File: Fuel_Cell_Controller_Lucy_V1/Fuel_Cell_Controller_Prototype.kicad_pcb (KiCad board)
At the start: 2 copper layers, 114 parts, among them J1 STD_PWR_HEADER, J2 SWD_HEADER, J3 DE9_Receptacle, J4 DA15_Receptacle_MountingHoles, J5 USB_B_Micro, Q1 SI2302A-TPMSCT-ND, Q2 SI2302A-TPMSCT-ND, Q3 FMMT491ATA, Q4 FMMT491ATA, SW1 PTS815 SJM 250 SMTR LFS, SW2 PTS815 SJM 250 SMTR LFS, U1 LD39050PU33R, U10 FT234XD-R, U11 MCP2542FD-E/SN, U12 USBLC6-2SC6, U13 EL3H7(B)(TA)-VG, U14 MCP602-E/SN, U2 LD39050PU33R, U3 STM32L432KCUx, U4 MAX14572, U5 MAX14572, U6 EL3H7(B)(TA)-VG, U7 MCP1501-33E/SN, U8 AD8603, U9 AD8603, X1 OXETDLJANF-8MHZ

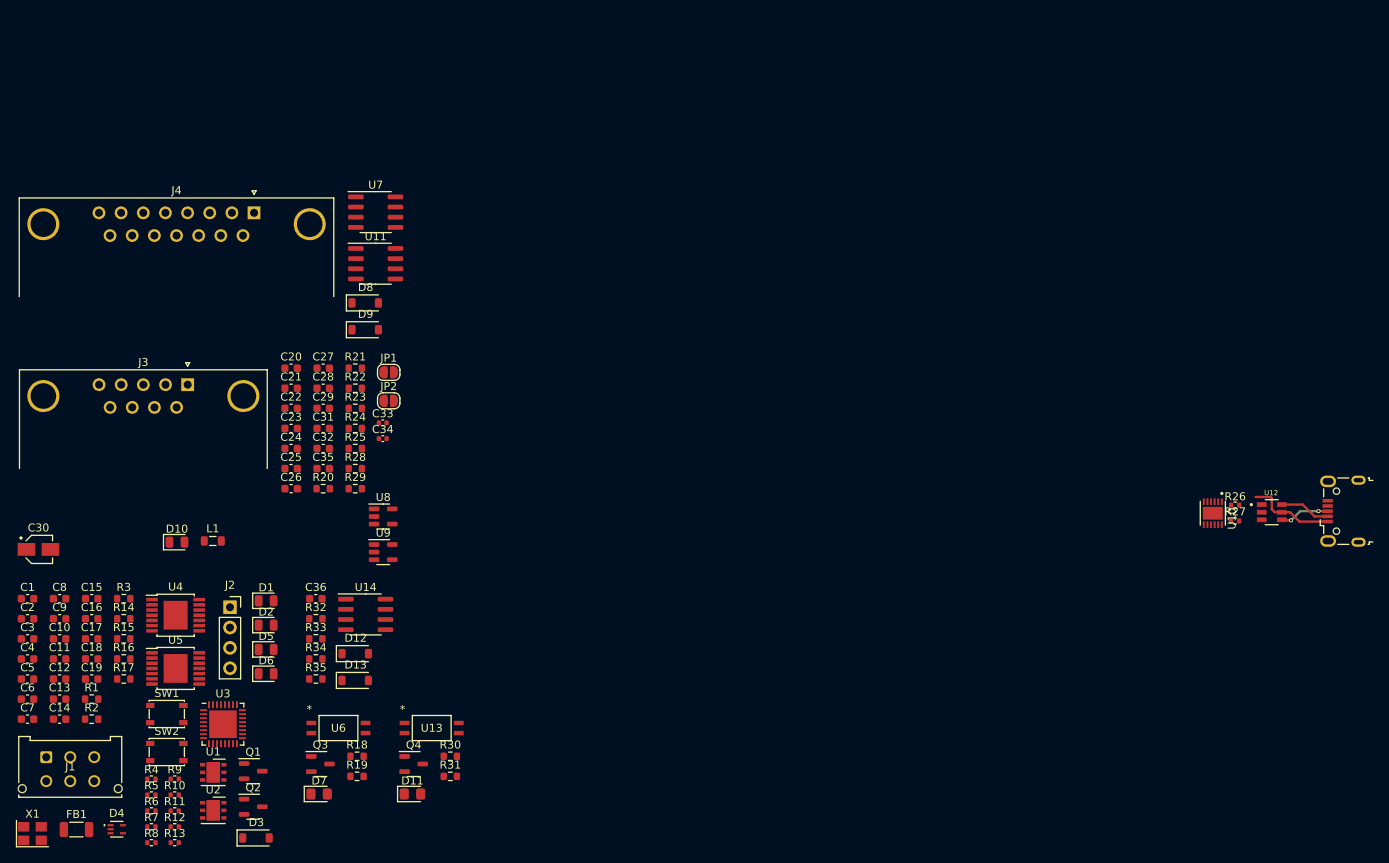
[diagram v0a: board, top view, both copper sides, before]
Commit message: Most of the schematic done, pcb layout needs DRC
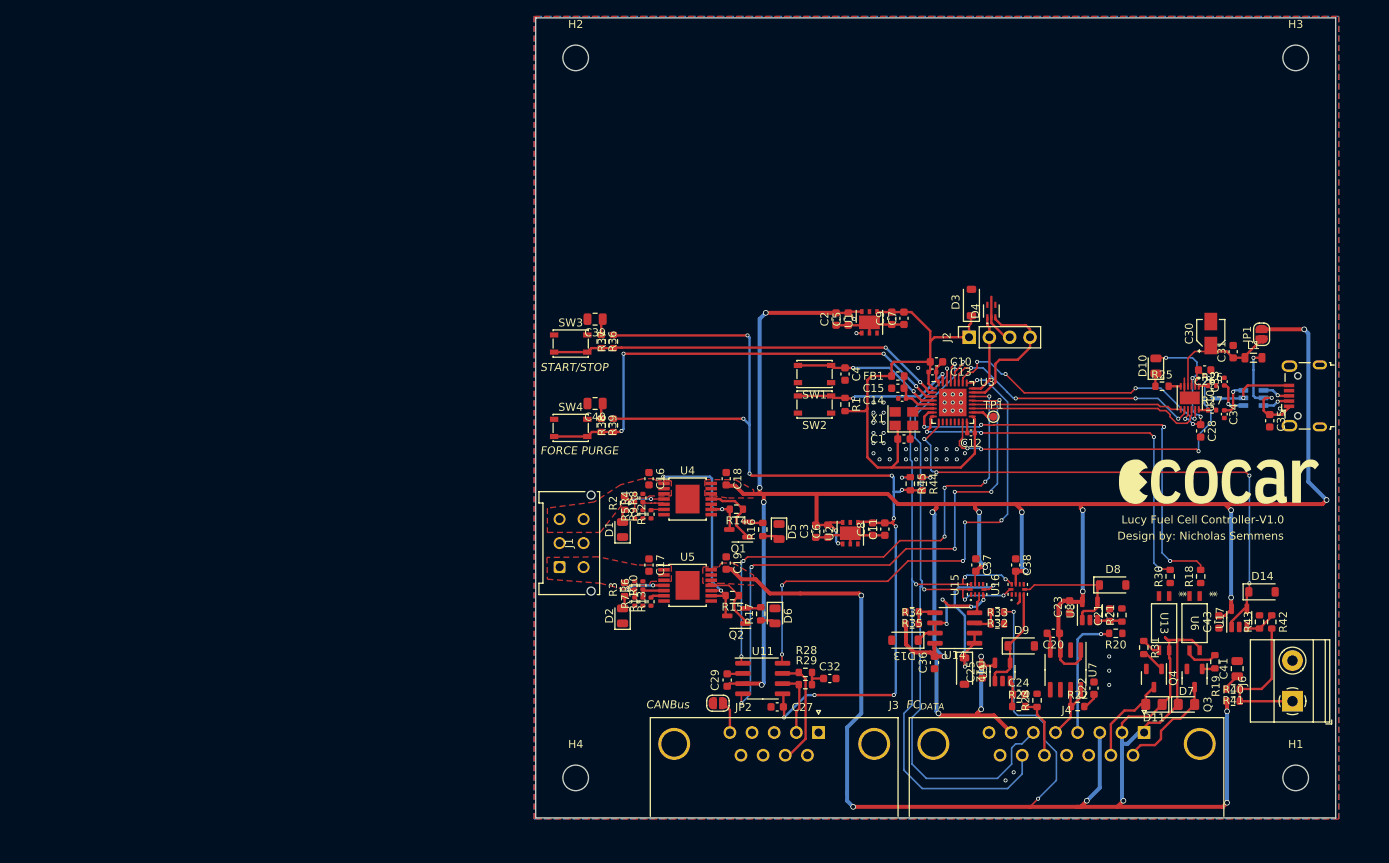
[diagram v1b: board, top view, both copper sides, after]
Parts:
- added C37: 100n, Capacitor_SMD:C_0603_1608Metric, F.Cu at (154.0, 104.4)
- added C38: 100n, Capacitor_SMD:C_0603_1608Metric, F.Cu at (159.0, 104.4)
- added C39: 3u, Capacitor_SMD:C_0805_2012Metric, F.Cu at (106.4, 73.7)
- added C40: 3u, Capacitor_SMD:C_0805_2012Metric, F.Cu at (106.4, 84.2)
- added C41: 3u, Capacitor_SMD:C_0805_2012Metric, F.Cu at (186.7, 117.3)
- added C43: 100n, Capacitor_SMD:C_0603_1608Metric, F.Cu at (184.4, 111.5)
- added D14: MMSZ5226B-7-F, FC.FTP:D_SOD_123_M, F.Cu at (189.7, 107.7)
- added G***: LOGO, RB_FTP:ecocar_logo, F.Cu at (184.4, 94.0)
- added H1: MountingHole, MountingHole:MountingHole_3.2mm_M3, F.Cu at (194.0, 131.0)
- added H2: MountingHole, MountingHole:MountingHole_3.2mm_M3, F.Cu at (104.0, 41.0)
- added H3: MountingHole, MountingHole:MountingHole_3.2mm_M3, F.Cu at (194.0, 41.0)
- added H4: MountingHole, MountingHole:MountingHole_3.2mm_M3, F.Cu at (104.0, 131.0)
- added J6: Screw_Terminal_01x02, TerminalBlock_Phoenix:TerminalBlock_Phoenix_MKDS-1,5-2-5.08_1x02_P5.08mm_Horizontal, F.Cu at (193.6, 121.4)
- added NT1: NetTie_2, NetTie:NetTie-2_SMD_Pad0.5mm, B.Cu at (184.2, 83.6)
- added R36: 10k, Resistor_SMD:R_0603_1608Metric, F.Cu at (107.2, 76.5)
- added R37: 10k, Resistor_SMD:R_0603_1608Metric, F.Cu at (108.7, 76.5)
- added R38: 10k, Resistor_SMD:R_0603_1608Metric, F.Cu at (108.7, 86.9)
- added R39: 10k, Resistor_SMD:R_0603_1608Metric, F.Cu at (107.2, 86.9)
- added R40: 10k, Resistor_SMD:R_0603_1608Metric, F.Cu at (186.2, 121.4)
- added R41: 10k, Resistor_SMD:R_0603_1608Metric, F.Cu at (186.2, 119.9)
- added R42: 1740, Resistor_SMD:R_0603_1608Metric, F.Cu at (191.0, 111.5)
- added R43: 660, Resistor_SMD:R_0603_1608Metric, F.Cu at (189.5, 111.5)
- added R44: 4.7k, Resistor_SMD:R_0603_1608Metric, F.Cu at (147.3, 94.2)
- added R45: 4.7k, Resistor_SMD:R_0603_1608Metric, F.Cu at (145.8, 94.2)
- added SW3: PTS815 SJM 250 SMTR LFS, Button_Switch_SMD:SW_SPST_PTS810, F.Cu at (103.4, 76.7)
- added SW4: PTS815 SJM 250 SMTR LFS, Button_Switch_SMD:SW_SPST_PTS810, F.Cu at (103.4, 87.3)
- added TP1: MCO, TestPoint:TestPoint_Pad_D1.0mm, F.Cu at (156.2, 85.9)
- added U15: ADS1115IRUGR, FC.FTP:IC_ADS1115IRUGR, F.Cu at (154.2, 107.4)
- added U16: ADS1115IRUGR, FC.FTP:IC_ADS1115IRUGR, F.Cu at (159.3, 107.4)
- added U17: AD8603, Package_TO_SOT_SMD:TSOT-23-5, F.Cu at (186.9, 111.0)
- C12, C13, C14: footprint Capacitor_SMD:C_0603_1608Metric -> Capacitor_SMD:C_0402_1005Metric
- C24: value 100n -> 1u
- FB1: footprint Inductor_SMD:L_1206_3216Metric -> Inductor_SMD:L_0603_1608Metric
- U12: moved to B.Cu
- moved C30 149.0 mm to (183.4, 75.5), turned to 90 degrees
- moved L1 132.1 mm to (188.7, 78.5)
- moved J4 128.8 mm to (175.1, 125.3)
- moved D4 127.1 mm to (156.0, 72.6), turned to 90 degrees
- moved D10 124.3 mm to (176.5, 79.5), turned to 90 degrees
- moved X1 120.6 mm to (145.0, 86.1)
- moved C7 120.5 mm to (145.0, 73.6), turned to 90 degrees
- moved C35 118.5 mm to (190.8, 86.4), turned to -90 degrees
- moved C12 118.0 mm to (153.4, 87.9), turned to 180 degrees
- moved FB1 117.3 mm to (144.3, 80.8)
- moved C13 116.5 mm to (148.6, 80.3)
- moved C26 115.2 mm to (182.6, 80.0), turned to 180 degrees
- moved C10 114.9 mm to (149.1, 79.0)
- moved C31 114.1 mm to (186.2, 77.7), turned to 90 degrees
- moved C14 112.7 mm to (144.8, 83.6), turned to 180 degrees
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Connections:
- net /On-Board Sensors/12V_Ref renamed /On-Board Sensors/12V_{REF}
- net /On-Board Sensors/5V_Ref renamed /On-Board Sensors/5V_{REF}
- C11 pad 1: GND -> GNDA
- C16 pad 1: GNDPWR -> GNDA
- C17 pad 1: GNDPWR -> GNDA
- C18 pad 1: GNDPWR -> GNDA
- C19 pad 1: GNDPWR -> GNDA
- C2 pad 1: GND -> GNDA
- C20 pad 2: GND -> GNDA
- C21 pad 2: GND -> GNDA
- C22 pad 2: GND -> GNDA
- C23 pad 1: GND -> GNDA
- C24 pad 2: GND -> GNDA
- C25 pad 1: GND -> GNDA
- C26 pad 1: GND -> GNDA
- C27 pad 2: GND -> GNDA
- C28 pad 2: GND -> GNDA
- C29 pad 1: GND -> GNDA
- C3 pad 1: GND -> GNDA
- C30 pad 2: GND -> GNDA
- C31 pad 2: GND -> GNDA
- C32 pad 1: GND -> GNDA
- C33 pad 2: GND -> GNDA
- C34 pad 2: GND -> GNDA
- C35 pad 2: GND -> GNDA
- C36 pad 1: GND -> GNDA
- C5 pad 1: GND -> GNDA
- C6 pad 1: GND -> GNDA
- C7 pad 1: GND -> GNDA
- C8 pad 1: GND -> GNDA
- C9 pad 1: GND -> GNDA
- D1 pad 1: GND -> GNDA
- D11 pad 1: UNPROTECTED_12V -> +12V
- D12 pad 2: GND -> GNDA
- D13 pad 2: GND -> GNDA
- D2 pad 1: GND -> GNDA
- D3 pad 1: +3V3 -> /MCU_3V3
- D4 pad 1: unconnected-(D4-Pad1) -> /IO /PA14
- D4 pad 3: unconnected-(D4-Pad3) -> /IO /PA13
- D4 pad 4: /IO /PA13 -> unconnected-(D4-Pad4)
- D4 pad 5: /IO /PA14 -> unconnected-(D4-Pad5)
- D5 pad 1: GND -> GNDA
- D6 pad 1: GND -> GNDA
- D7 pad 1: UNPROTECTED_12V -> +12V
- D8 pad 1: /IO /PA3 -> /IO /H2_{PRS}
- D8 pad 2: GND -> GNDA
- D9 pad 1: /IO /PA4 -> /IO /FC_{TEMP}
- D9 pad 2: GND -> GNDA
- J1 pad 2: GND -> GNDA
- J1 pad 5: GND -> GNDA
- J2 pad 1: +3V3 -> /MCU_3V3
- J3 pad 0: GND -> GNDA
- J3 pad 6: GND -> /IO /GND
- J4 pad 0: GND -> GNDA
- J4 pad 1: UNPROTECTED_12V -> +12V
- J4 pad 11: /IO /PRESSURE_PWR- -> GNDA
- J4 pad 14: unconnected-(J4-P14-Pad14) -> /IO /PB7
- J4 pad 15: GND -> GNDA
- J4 pad 2: UNPROTECTED_12V -> +12V
- J4 pad 3: /IO /PRESSURE_PWR+ -> +12V
- J4 pad 6: unconnected-(J4-Pad6) -> /IO /PB6
- J4 pad 7: unconnected-(J4-Pad7) -> +5V
- J4 pad 8: GND -> GNDA
- J5 pad 5: GND -> /IO /GND_{1}
- J5 pad 6: GND -> GNDA
- JP2 pad 1: GND -> GNDA
- R1 pad 1: +3V3 -> /BOOT0
- R1 pad 2: /BOOT0 -> /MCU_3V3
- R11 pad 1: GND -> GNDA
- R12 pad 1: GND -> GNDA
- R13 pad 1: GND -> GNDA
- R21 pad 2: GND -> GNDA
- R23 pad 2: GND -> GNDA
- R33 pad 2: GND -> GNDA
- R35 pad 2: GND -> GNDA
- R5 pad 1: GND -> GNDA
- R7 pad 1: GND -> GNDA
- R9 pad 1: GND -> GNDA
- U1 pad 2: GND -> GNDA
- U1 pad 7: GND -> GNDA
- U10 pad 13: GND -> GNDA
- U10 pad 5: GND -> GNDA
- U11 pad 2: GND -> GNDA
- U12 pad 2: GND -> /IO /GND_{1}
- U13 pad 4: UNPROTECTED_12V -> +12V
- U14 pad 4: GND -> GNDA
- U2 pad 2: GND -> GNDA
- U2 pad 7: GND -> GNDA
- U3 pad 2: unconnected-(U3-PC14-Pad2) -> /PC14
- U3 pad 3: unconnected-(U3-PC15-Pad3) -> /PC15
- U4 pad 15: GND -> GNDA
- U4 pad 7: GND -> GNDA
- U4 pad 8: GND -> GNDA
- U5 pad 10: UNPROTECTED_12V -> UNPROTECTED_5V
- U5 pad 15: GND -> GNDA
- U5 pad 7: GND -> GNDA
- U5 pad 8: GND -> GNDA
- U5 pad 9: UNPROTECTED_12V -> UNPROTECTED_5V
- U6 pad 4: UNPROTECTED_12V -> +12V
- U7 pad 2: GND -> GNDA
- U7 pad 4: GND -> GNDA
- U7 pad 5: GND -> GNDA
- U7 pad 6: GND -> GNDA
- U8 pad 1: /IO /PA3 -> /IO /H2_{PRS}
- U8 pad 2: GND -> GNDA
- U8 pad 4: /IO /PA3 -> /IO /H2_{PRS}
- U9 pad 1: /IO /PA4 -> /IO /FC_{TEMP}
- U9 pad 2: GND -> GNDA
- U9 pad 4: /IO /PA4 -> /IO /FC_{TEMP}
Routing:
- net +5V: track 0.00 -> 304.1 mm, vias 0 -> 23
- net +12V: track 0.00 -> 196.4 mm, vias 0 -> 8
- net +3V3: track 0.00 -> 123.3 mm, vias 0 -> 10
- net /IO /PB6: track 0.00 -> 91.8 mm, vias 0 -> 5
- net /IO /PB7: track 0.00 -> 90.7 mm, vias 0 -> 5
- net /IO /PA11: track 0.00 -> 72.2 mm, vias 0 -> 6
- net /MCU_3V3: track 0.00 -> 70.5 mm
- net /IO /PA3: track 0.00 -> 67.3 mm, vias 0 -> 4
- net /IO /PA15: track 0.00 -> 64.7 mm, vias 0 -> 6
- net /IO /PA12: track 0.00 -> 63.9 mm, vias 0 -> 6
- net /PC15: track 0.00 -> 59.4 mm, vias 0 -> 4
- net /IO /PA1: track 0.00 -> 54.7 mm, vias 0 -> 4
- net /PC14: track 0.00 -> 50.1 mm, vias 0 -> 2
- net /IO /PA2: track 0.00 -> 49.1 mm, vias 0 -> 4
- net /IO /PB1: track 0.00 -> 47.5 mm, vias 0 -> 4
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- added copper zone on F.Cu, net +12V
- added copper zone on F.Cu, net +5V
- added copper zone on B.Cu, net GNDA
- added copper zone on F.Cu, net GNDA
- added copper zone on F.Cu, net UNPROTECTED_12V
- added copper zone on F.Cu, net UNPROTECTED_5V
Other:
- board outline added: 100 x 100 mm
- board text added: "${COMMENT1}"
- board text added: "${TITLE}-${REVISION}"
- board text added: "CANBus"
- board text added: "FC_{DATA}"
- board text added: "FORCE PURGE"
- board text added: "START/STOP"

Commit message: So much again
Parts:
- added C42: 100n, Capacitor_SMD:C_0603_1608Metric, F.Cu at (133.8, 90.6)
- added C45: 10u, Capacitor_SMD:CP_Elec_3x5.3, F.Cu at (130.6, 88.1)
- added Display 128x64 0.96" I2C: Display_128x64, FC.FTP:Display_128x64_096_I2C, F.Cu at (166.4, 92.5)
- added J7: OLED, Connector_PinSocket_2.54mm:PinSocket_1x04_P2.54mm_Vertical, F.Cu at (162.6, 92.4)
- added U18: LIS3DHTR, FC.FTP:XDCR_LIS3DHTR, F.Cu at (137.1, 89.6)
- moved G*** 67.1 mm to (123.0, 67.0)
- moved H2 28.0 mm to (104.0, 69.0)
- moved H3 28.0 mm to (194.0, 69.0)
- moved C1 3.02 mm to (142.1, 87.9), turned to -90 degrees
- moved D3 2.13 mm to (151.8, 73.0), turned to 180 degrees
- moved C39 1.74 mm to (108.2, 73.9), turned to 0 degrees
- moved C40 1.73 mm to (108.2, 84.4), turned to 0 degrees
- moved C28 0.25 mm to (182.4, 87.6)
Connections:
- net /PC14 renamed /BTN_{1}
- net /PC15 renamed /BTN_{2}
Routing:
- net /IO /PB6: track 91.8 -> 128.7 mm, vias 5 -> 6
- net /IO /PB7: track 90.7 -> 127.4 mm, vias 5 -> 6
- net +5V: track 304.1 -> 325.5 mm, vias 23 -> 28
- net /IO /PA4: track 0.00 -> 19.4 mm, vias 0 -> 2
- net /IO /PA5: track 0.00 -> 16.8 mm, vias 0 -> 2
- net +3V3: track 123.3 -> 138.1 mm
- net /BOOT0: track 20.6 -> 30.9 mm, vias 2 -> 4
- net /MCU_3V3: track 70.5 -> 60.4 mm, vias 0 -> 4
- net /IO /PB5: track 3.06 -> 0.00 mm, vias 1 -> 0
- net /IO /PB4: track 33.1 -> 35.4 mm
- net GNDA: track 44.0 -> 46.0 mm, vias 44 -> 218
- net Net-(R30-Pad1): track 0.00 -> 1.68 mm
- net Net-(R18-Pad1): track 0.00 -> 1.68 mm
- net Net-(U8-+): track 3.03 -> 4.52 mm
- net /On-Board Sensors/5V_{REF}: track 15.0 -> 16.4 mm
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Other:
- board size 100 x 100 mm -> 100 x 73 mm
- board text added: "BOOT0"
- board text added: "~{RST}"

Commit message: $
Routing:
- net /MCU_3V3: track 60.4 -> 61.1 mm, vias 4 -> 5
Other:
- board text added: "~{FAULT}"
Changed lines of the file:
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@@
     (effects (font (size 1 1) (thickness 0.15) italic) (justify left bottom))
+  )
+  (gr_text "~{FAULT}" (at 131.953 113.157 90) (layer "F.SilkS")
+    (effects (font (size 1 1) (thickness 0.2) bold italic) (justify left bottom))
   )
   (gr_text "${COMMENT1}" (at 110.3 74.366) (layer "F.SilkS")
@@
   (gr_text "CANBus" (at 112.776 122.428) (layer "F.SilkS")
     (effects (font (size 1 1) (thickness 0.15) italic) (justify left bottom))
+  )
+  (gr_text "~{FAULT}" (at 132.461 102.489 90) (layer "F.SilkS")
+    (effects (font (size 1 1) (thickness 0.2) bold italic) (justify left bottom))
   )
   (gr_text "FORCE PURGE" (at 99.568 90.678) (layer "F.SilkS")
@@
   (segment (start 141.723 72.776) (end 141.666 72.719) (width 0.3) (layer "F.Cu") (net 1))
   (segment (start 143.4845 79.2735) (end 143.4845 80.772) (width 0.3) (layer "F.Cu") (net 1))
+  (segment (start 149.391 75.145) (end 148.323 75.145) (width 0.3) (layer "F.Cu") (net 1))
   (segment (start 153.172 73.1185) (end 153.3671 72.9234) (width 0.3) (layer "F.Cu") (net 1))
   (segment (start 148.3234 75.921) (end 148.323 75.9206) (width 0.3) (layer "F.Cu") (net 1))
   (segment (start 153.172 75.921) (end 153.172 73.1185) (width 0.3) (layer "F.Cu") (net 1))
+  (segment (start 149.86 74.676) (end 149.391 75.145) (width 0.3) (layer "F.Cu") (net 1))
   (segment (start 137.6802 85.1408) (end 137.668 85.153) (width 0.3) (layer "F.Cu") (net 1))
   (segment (start 148.11 81.7415) (end 148.6925 82.324) (width 0.3) (layer "F.Cu") (net 1))
@@
   (segment (start 148.323 75.145) (end 145.954 72.776) (width 0.3) (layer "F.Cu") (net 1))
   (segment (start 148.323 76.454) (end 148.323 75.145) (width 0.3) (layer "F.Cu") (net 1))
-  (segment (start 153.172 75.921) (end 148.3234 75.921) (width 0.3) (layer "F.Cu") (net 1))
   (segment (start 143.781 87.109) (end 143.934 86.956) (width 0.3) (layer "F.Cu") (net 1))
   (via (at 140.462 80.772) (size 0.5) (drill 0.3) (layers "F.Cu" "B.Cu") (net 1))
+  (via (at 149.86 74.676) (size 0.8) (drill 0.4) (layers "F.Cu" "B.Cu") (net 1))
   (via (at 153.8732 86.487) (size 0.5) (drill 0.3) (layers "F.Cu" "B.Cu") (net 1))
   (via (at 140.462 85.1408) (size 0.5) (drill 0.3) (layers "F.Cu" "B.Cu") (net 1))
@@
   (segment (start 140.462 80.772) (end 140.462 85.1408) (width 0.3) (layer "B.Cu") (net 1))
   (segment (start 153.172 75.921) (end 153.172 85.7858) (width 0.2) (layer "B.Cu") (net 1))
+  (segment (start 149.86 74.676) (end 150.114 74.676) (width 0.3) (layer "B.Cu") (net 1))
+  (segment (start 150.114 74.676) (end 151.359 75.921) (width 0.3) (layer "B.Cu") (net 1))
   (segment (start 140.462 86.995) (end 140.589 87.122) (width 0.3) (layer "B.Cu") (net 1))
   (segment (start 153.172 85.7858) (end 153.8732 86.487) (width 0.2) (layer "B.Cu") (net 1))
+  (segment (start 151.359 75.921) (end 153.172 75.921) (width 0.3) (layer "B.Cu") (net 1))
   (segment (start 138.176 87.249) (end 138.303 87.63) (width 0.3) (layer "F.Cu") (net 2))
   (segment (start 159.258 109.22) (end 159.508 108.97) (width 0.3) (layer "F.Cu") (net 2))

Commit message: I really shouldn't be pushing so much but oh well
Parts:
- added C44: 3u, Capacitor_SMD:C_0805_2012Metric, F.Cu at (184.7, 101.2)
- added J8: Screw_Terminal_01x02, TerminalBlock_Phoenix:TerminalBlock_Phoenix_MKDS-1,5-2-5.08_1x02_P5.08mm_Horizontal, F.Cu at (193.8, 103.0)
- added R47: 10k, Resistor_SMD:R_0603_1608Metric, F.Cu at (187.2, 102.0)
- C35: value 10n -> 100n
- R16, R17, R2: value 10k -> 270
- R23: value 10k -> 100k
- R3: value 10k -> 500
- SW3, SW4: value PTS815 SJM 250 SMTR LFS -> ~; footprint Button_Switch_SMD:SW_SPST_PTS810 -> Button_Switch_THT:SW_PUSH_6mm_H5mm
- moved R36 4.74 mm to (109.7, 80.5)
- moved R37 4.74 mm to (111.2, 80.5)
- moved C39 4.74 mm to (110.7, 77.9)
- moved SW4 2.97 mm to (100.9, 85.6)
- moved C40 2.65 mm to (110.7, 85.1)
- moved R38 2.65 mm to (111.3, 87.7)
- moved R39 2.65 mm to (109.7, 87.7)
- moved SW3 2.59 mm to (100.9, 76.0)
- moved NT1 0.63 mm to (184.5, 83.1)
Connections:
- J4 pad 13: /IO /THERM_{RTN} -> GNDA
- R22 pad 1: /IO /THERM_{VREF} -> Net-(U7-FB)
- R23 pad 1: /IO /THERM_{RTN} -> Net-(U7-FB)
- R23 pad 2: GNDA -> /IO /THERM_{VREF}
- R24 pad 2: /IO /THERM_{RTN} -> /IO /THERM_{VREF}
- U7 pad 7: /IO /THERM_{VREF} -> Net-(U7-FB)
- U7 pad 8: /IO /THERM_{VREF} -> Net-(U7-FB)
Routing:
- net /IO /PA6: track 0.00 -> 59.7 mm, vias 0 -> 4
- net +3V3: track 138.1 -> 129.5 mm
- net Net-(U7-FB): track 0.00 -> 8.32 mm
- net /IO /THERM_{RTN}: track 7.90 -> 0.00 mm
- net +12V: track 196.4 -> 203.6 mm, vias 8 -> 10
- net /BTN_{1}: track 50.7 -> 55.3 mm, vias 2 -> 4
- net +5V: track 325.5 -> 321.6 mm
- net Net-(C44-Pad1): track 0.00 -> 1.62 mm
- net /BTN_{2}: track 59.4 -> 60.7 mm
- net /IO /PA15: track 64.7 -> 65.3 mm
- net /MCU_3V3: track 61.1 -> 61.7 mm
- net /IO /FC_{TEMP}: track 13.3 -> 13.8 mm
- net GNDA: track 46.0 -> 45.6 mm, vias 218 -> 219
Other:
- board text added: "5V ⏚ 12V 5V ⏚ 12V"
- board text added: "Battery In"
- board text added: "FC_{CNTRL}"
- board text added: "SHELL_{STP}"
- board text removed: "FC_{DATA}"

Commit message: updated
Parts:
- C2, C3, C7, C8: value 1u_X5R -> 1u
- C21: value 100n -> 0u33
- C39, C40, C41, C44: value 3u -> 3u3
- D1, D2: value BLUE -> ICE BLUE
- D10: value LED -> PINK
- J2: value SWD_HEADER -> Conn_02x05_Odd_Even; footprint Connector_PinSocket_2.54mm:PinSocket_1x04_P2.54mm_Vertical -> Connector_PinSocket_2.54mm:PinSocket_2x05_P2.54mm_Vertical
- R11: value 225k -> 226k
- R20: value 10k -> 6.98k
- R21: value 10k -> 13.7k
- R22: value 50 -> 49.9
- R25: value 270 -> 30.1
- R26, R27: value 27 -> 26.7
- R28, R29: value 60 -> 60.4
- R3: value 500 -> 931
- R34, R35: value 100k -> 13.7k
- R43: value 660 -> 665
- R5: value 950k -> 953k
- R7: value 270k -> 267k
- R9: value 550k -> 549k
- moved J2 10.2 mm to (163.3, 75.9), turned to -90 degrees
- moved D4 7.41 mm to (159.8, 79.0), turned to 180 degrees
- moved D3 1.99 mm to (149.9, 73.5), turned to 90 degrees
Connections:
- D4 pad 1: /IO /PA14 -> /~{RST}
- D4 pad 3: /IO /PA13 -> /SW_{IM}
- D4 pad 4: unconnected-(D4-Pad4) -> /IO /PA14
- D4 pad 5: unconnected-(D4-Pad5) -> /IO /PA13
- J2 pad 1: /MCU_3V3 -> /~{RST}
- J2 pad 2: /IO /PA14 -> /IO /PA13
- J2 pad 4: /IO /PA13 -> GNDA
- R1 pad 1: /BOOT0 -> GNDA
- R1 pad 2: /MCU_3V3 -> /BOOT0
- SW2 pad 1: GNDA -> /BOOT0
- SW2 pad 2: /BOOT0 -> /MCU_3V3
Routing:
- net UNPROTECTED_5V: track 35.3 -> 125.7 mm, vias 3 -> 5
- net /~{RST}: track 19.4 -> 77.5 mm, vias 2 -> 5
- net /MCU_3V3: track 61.7 -> 66.1 mm
- net GNDA: track 45.6 -> 41.2 mm, vias 219 -> 218
- net /IO /PA14: track 10.5 -> 14.7 mm
- net /SW_{IM}: track 0.00 -> 3.57 mm, vias 0 -> 1
- net /IO /PA13: track 18.3 -> 16.9 mm
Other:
- board text added: "T_{X}\R_{X}"
